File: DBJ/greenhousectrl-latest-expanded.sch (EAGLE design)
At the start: 56 parts, among them IC1 ATMEGA168TQFP-08, IC4 L298, J1 POWER_JACKPTH, K1 RELAYPTH4, Q1 MMBT2222A, U2 V_REG_317SMD, X1 CRYSTALS-NOGND-HC49

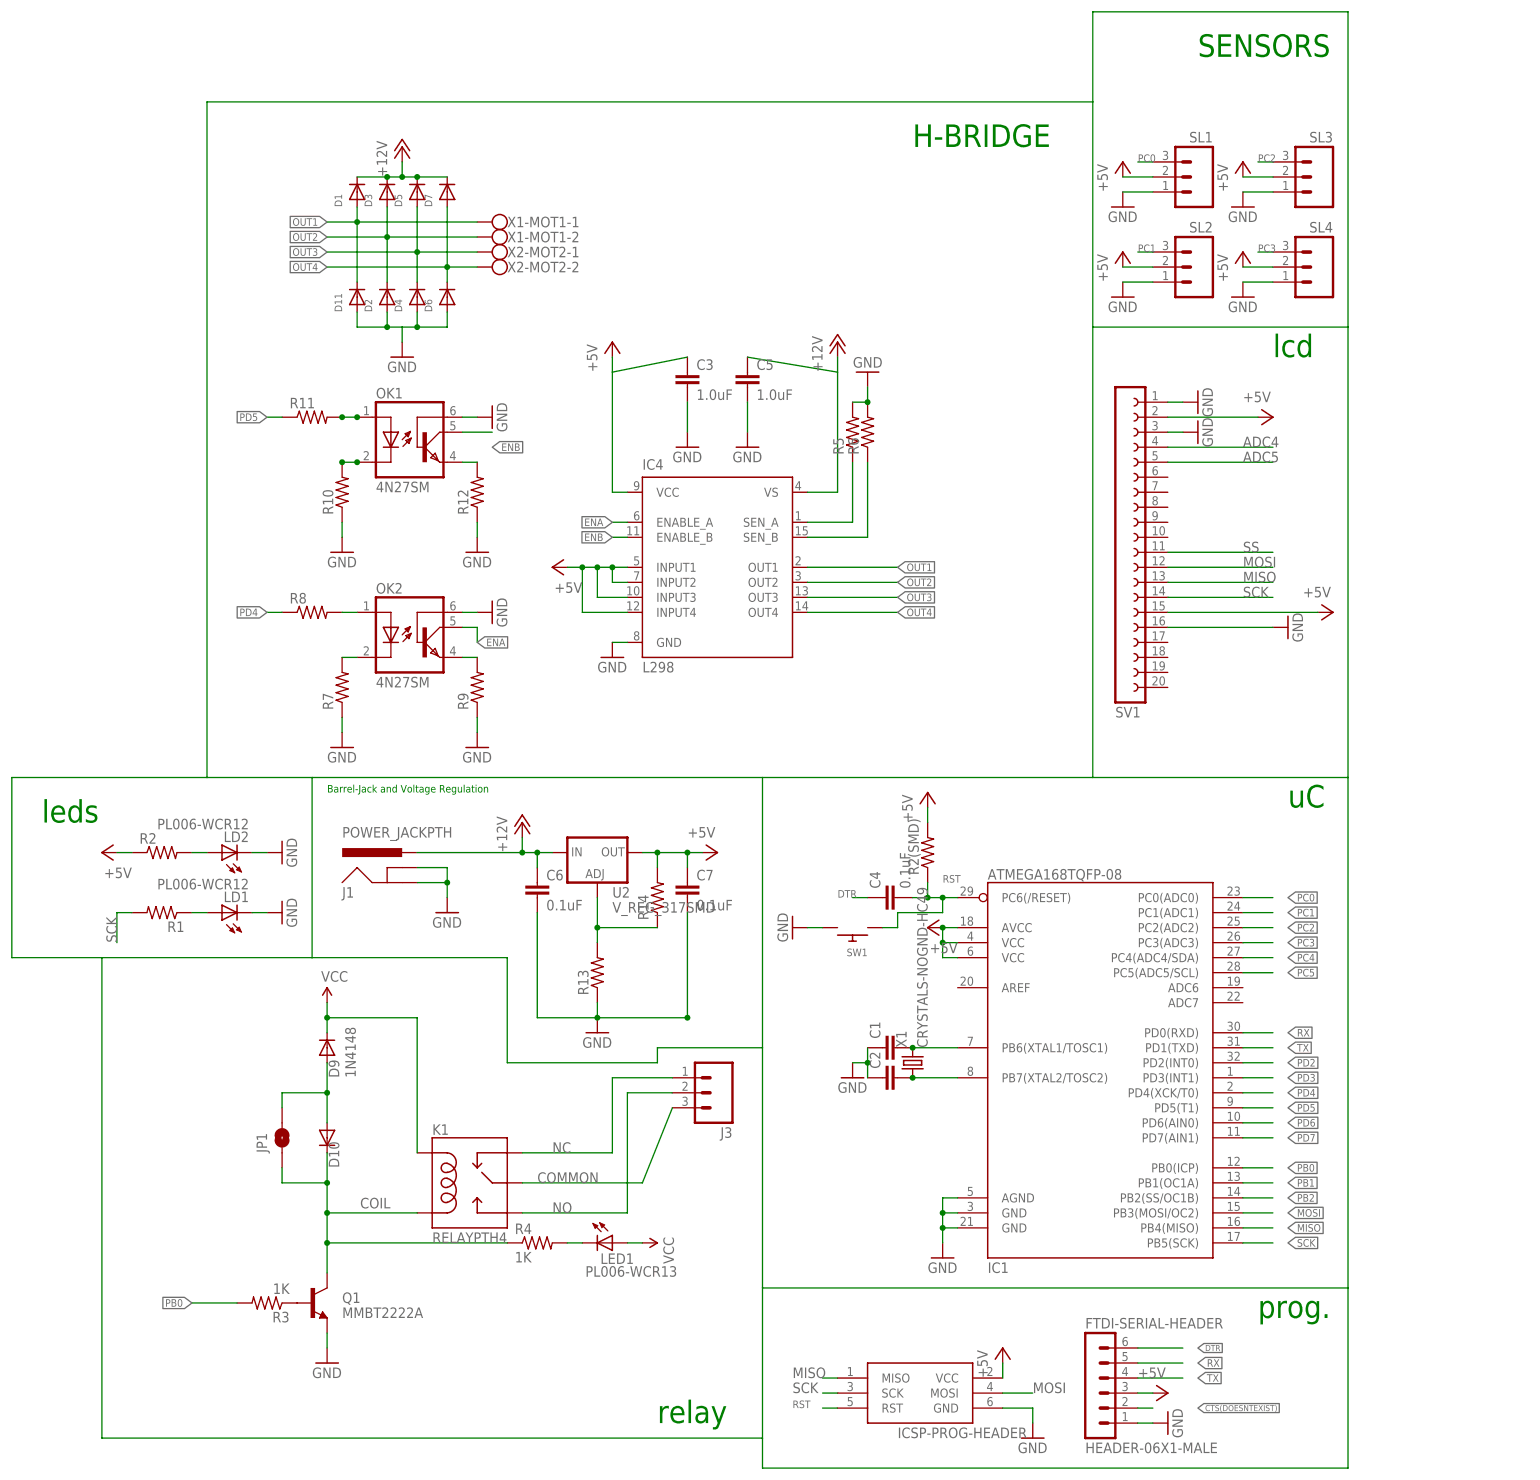
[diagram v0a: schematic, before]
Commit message: replaced parts to conform with preferred part list
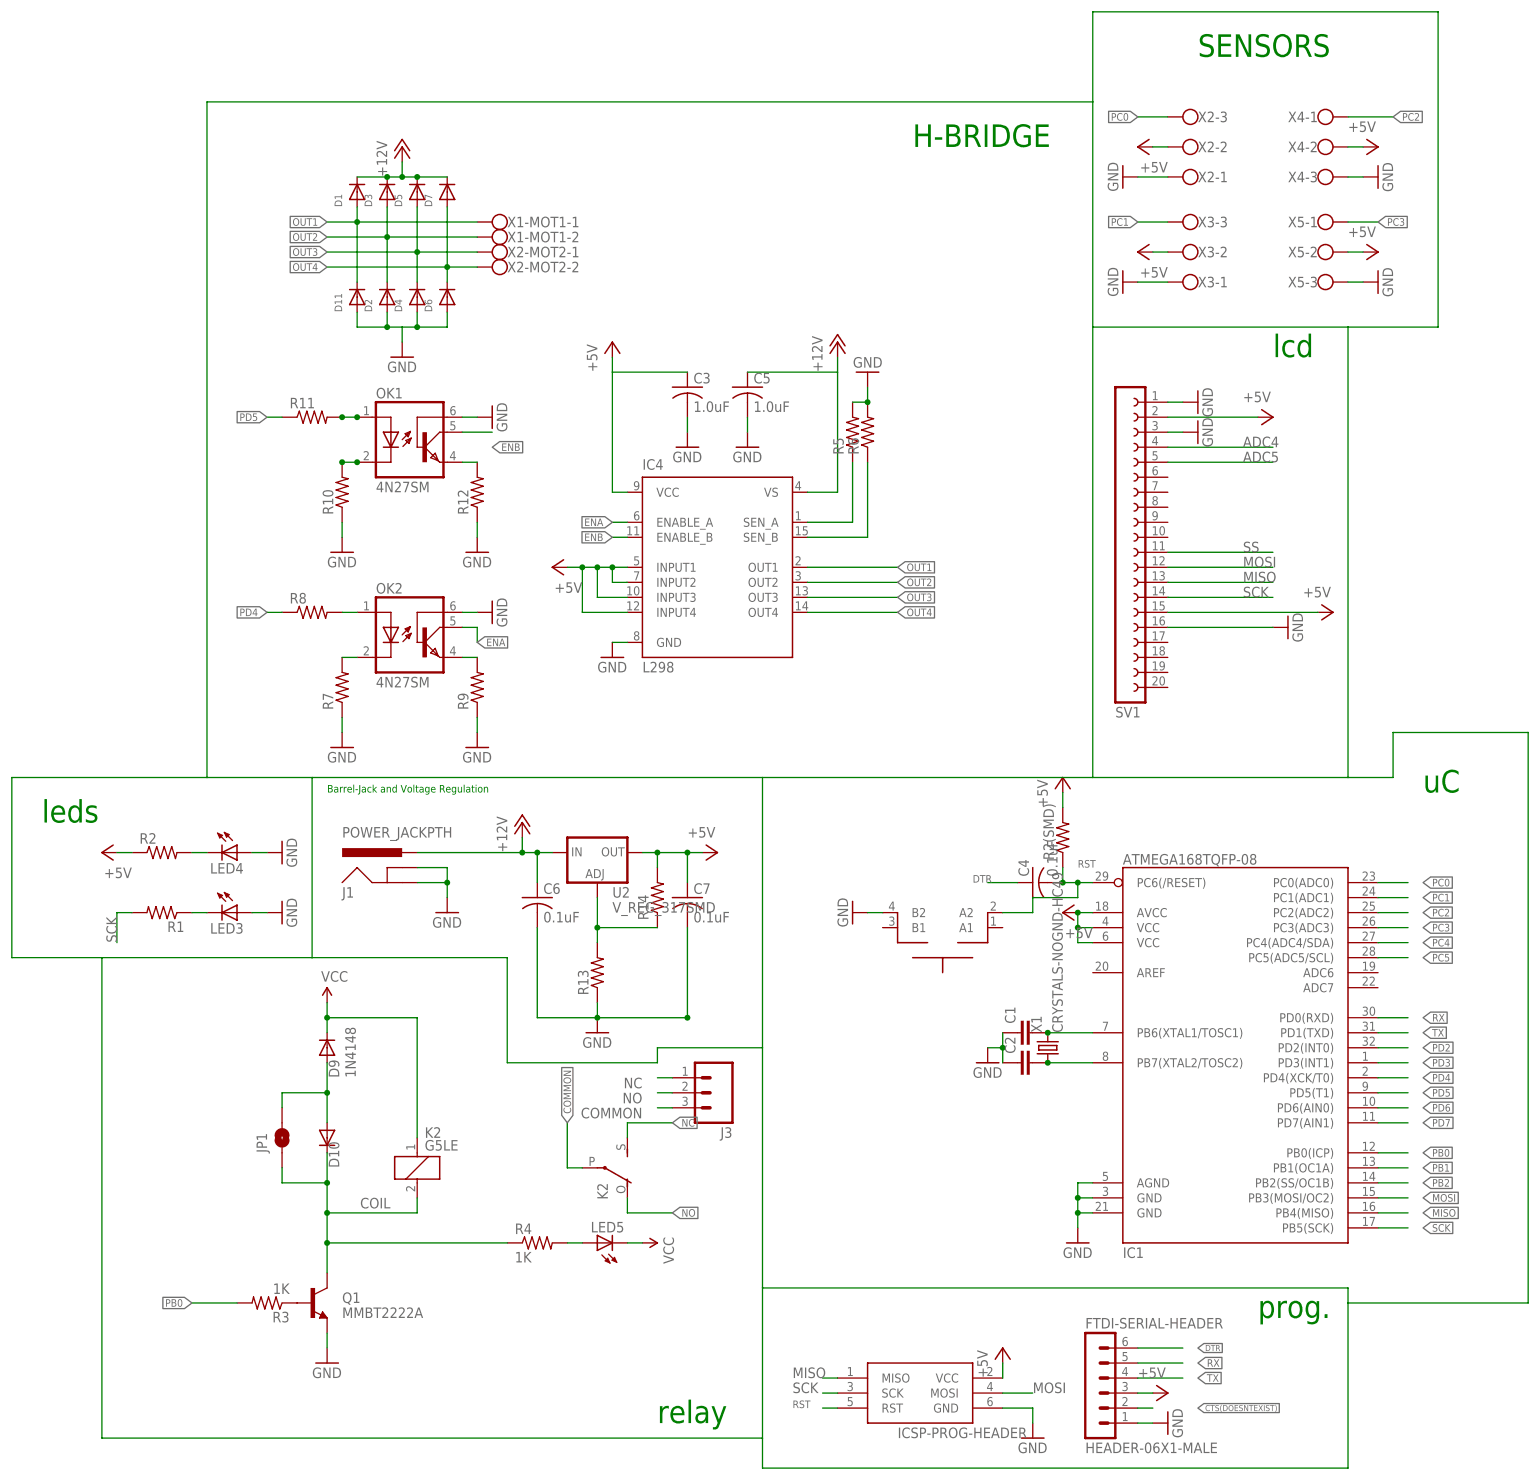
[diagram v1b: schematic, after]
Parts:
- removed K1: RELAYPTH4, SparkFun-Electromechanical:RELAYPTH4
- removed LD1, LD2: PL006-WCR12, led:PL006-WCR12
- removed LED1: PL006-WCR13, led:PL006-WCR13
- removed SL1, SL2, SL3, SL4: (no value), con-amp-quick:M03
- removed SW1: (no value), adafruit:SWITCH_PUSHBUTTONC&K_KSS
- added K2: G5LE, relay:G5LE
- added LED3, LED4, LED5: (no value), adafruit:LEDCHIP-LED0805
- added SW2: MOMENTARYBUTTON, ece388:MOMENTARYBUTTON
- added X2, X3, X4, X5: (no value), ece388:1X03_5MM_SCREW
- C3, C5: device SparkFun-Capacitors:1.0UF-25V-+80/-20(0805)" -> adafruit:C-USC0805
- C4, C6, C7: device SparkFun-Capacitors:0.1UF-25V(+80/-20%)(0603) -> adafruit:C-USC0805
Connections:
- net +5V: now also X2-2.KL, X3-2.KL, X4-2.KL, X5-2.KL; no longer SL1.2, SL2.2, SL3.2, SL4.2
- net COIL: now also K21.2; no longer K1.COIL2
- net COMMON: now also K22.P; no longer K1.MAIN
- net GND: now also LED3.A, LED4.A, SW2.B2, X2-1.KL, X3-1.KL, X4-3.KL, X5-3.KL; no longer LD1.C, LD2.C, SL1.1, SL2.1, SL3.1, SL4.1, SW1.P$2
- net N$10: now also LED3.C; no longer LD1.A
- net N$2: now also LED4.C; no longer LD2.A
- net N$3: now also LED5.A; no longer LED1.C
- net NC: now also K22.S; no longer K1.NC
- net NO: now also K22.O; no longer K1.NO
- net PC0: now also X2-3.KL; no longer SL1.3
- net PC1: now also X3-3.KL; no longer SL2.3
- net PC2: now also X4-1.KL; no longer SL3.3
- net PC3: now also X5-1.KL; no longer SL4.3
- net RST: now also SW2.A2; no longer SW1.P$1
- net VCC: now also K21.1, LED5.C; no longer K1.COIL1, LED1.A
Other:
- moved on the sheet: C1, C2, C3, C4, C5, C6, C7, IC1, R2(SMD), X1
